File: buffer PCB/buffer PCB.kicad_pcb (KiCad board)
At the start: 2 copper layers, 46.4 x 61.6 mm, 28 parts, among them J1 Conn_02x10_Odd_Even, J2 Conn_01x09, J3 Conn_01x09, J4 Conn_02x10_Odd_Even, U1 74HC245, U2 74HC245

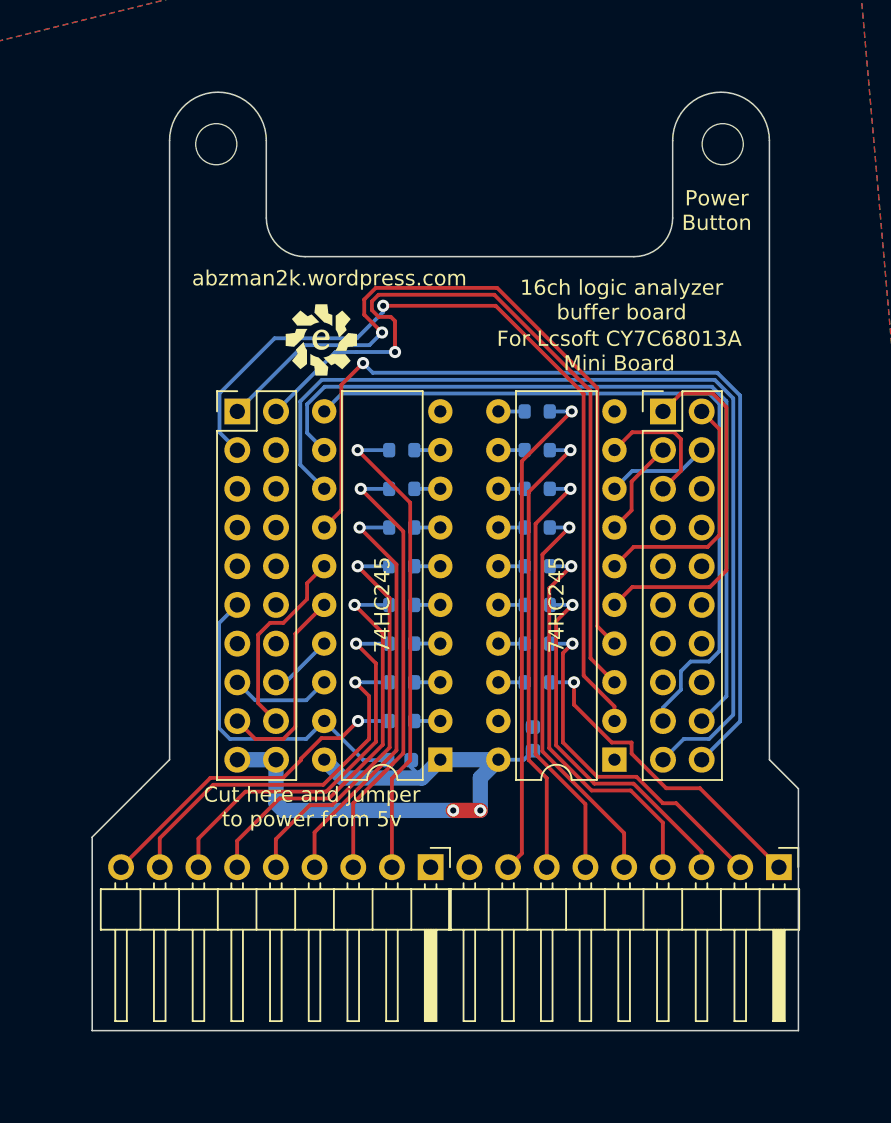
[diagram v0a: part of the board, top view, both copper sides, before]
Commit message: updated for different board power pinout and proper hole locations
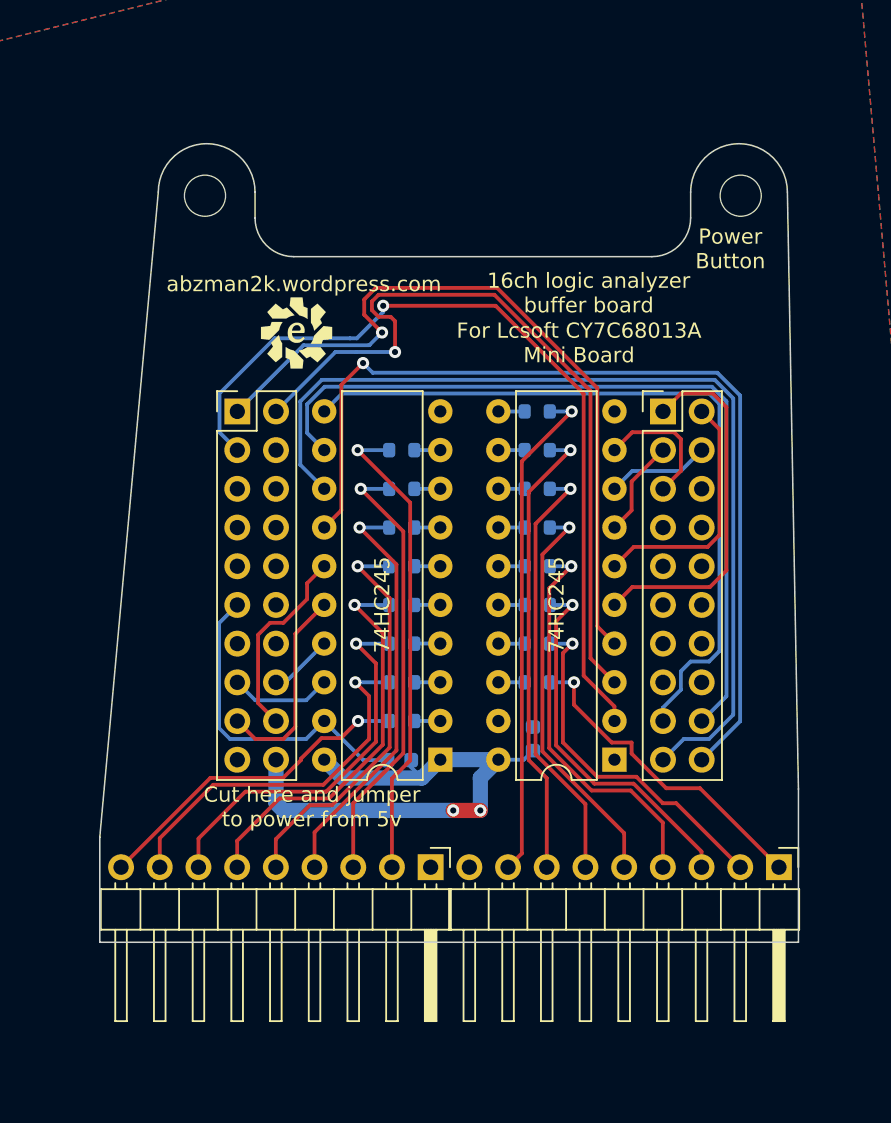
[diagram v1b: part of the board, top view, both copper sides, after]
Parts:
- moved REF** 3.58 mm to (137.2, 74.7)
- moved REF** 3.46 mm to (102.0, 74.7)
- moved G*** 1.69 mm to (108.0, 83.7)
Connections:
- J1 pad 10: GND -> unconnected-(J1-Pad10)
- J1 pad 19: +3V3 -> unconnected-(J1-Pad19)
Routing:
- net +3V3: track 39.2 -> 36.7 mm
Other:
- board size 46.4 x 61.6 mm -> 45.9 x 52.4 mm
